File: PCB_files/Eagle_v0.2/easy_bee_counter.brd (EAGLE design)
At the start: 373.4 x 34.5 mm, 123 parts, among them Q6 60V/32A/35mΩ, Q7 60V/32A/35mΩ

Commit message: Converted Logo to library part Added vias to be solded bridged for jumpers to bypass the SIP resistors. Rerouted the board, realigned many of the parts.
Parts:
- added U$44: BEE_LOGO, owen_desktop:BEE_LOGO
- C7: value 1uF -> 0.1uF
- J1: value (none) -> S_5V
- J3: value (none) -> S_LOAD
- J4: value (none) -> S_I2C
- R11, R12, R2, R5, R6, R7: value (none) -> 100KΩ
- U$34, U$35, U$36, U$37: value RPACK-BUSSED-9 -> 22Ω
- U1, U2, U3, U4, U5, U6: value (none) -> 74*165
- U7: value (none) -> R78E3.3-1.0; device SparkFun-IC-Power:TO220-IGO -> SparkFun-IC-Power:DC-DC_CONVERTER_78XX
- moved R11 0.90 mm to (184.2, 6.99)
- moved U$113 0.76 mm to (157.1, 22.3)
- moved U$112 0.76 mm to (157.1, 18.2)
- moved U$100 0.75 mm to (233.3, 18.2)
- moved U$101 0.75 mm to (233.3, 22.3)
- moved U$98 0.67 mm to (246.0, 18.2)
- moved U$99 0.67 mm to (246.0, 22.3)
- moved U$109 0.65 mm to (182.5, 22.3)
- moved U$108 0.65 mm to (182.5, 18.2)
- moved U$80 0.62 mm to (360.3, 18.2)
- moved U$81 0.62 mm to (360.3, 22.3)
- moved U$107 0.61 mm to (195.2, 22.3)
- moved U$106 0.61 mm to (195.2, 18.2)
- moved U$96 0.60 mm to (258.7, 18.2)
- moved U$97 0.60 mm to (258.7, 22.3)
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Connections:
- removed net N$44: U$45.MOSI
- net 3.3V: now also U7.VOUT; no longer U7.OUT
- net 5V: now also U7.VIN; no longer U7.IN
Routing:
- net GND: track 773.0 -> 561.9 mm, vias 4 -> 1
- net 3.3V: track 734.0 -> 812.3 mm
- net N$112: track 68.9 -> 43.3 mm
- net N$141: track 66.1 -> 47.2 mm, vias 0 -> 2
- net N$40: track 66.4 -> 49.4 mm, vias 0 -> 1
- net N$35: track 64.2 -> 47.2 mm, vias 0 -> 1
- net N$108: track 57.1 -> 40.6 mm, vias 1 -> 0
- net N$43: track 60.6 -> 46.9 mm, vias 0 -> 1
- net N$105: track 46.5 -> 33.0 mm
- net N$12: track 40.8 -> 52.7 mm, vias 1 -> 0
- net N$117: track 51.2 -> 39.8 mm, vias 2 -> 0
- net N$27: track 37.4 -> 47.9 mm
- net N$93: track 43.9 -> 35.2 mm, vias 2 -> 0
- net SCL: track 77.8 -> 69.1 mm
- net N$37: track 42.6 -> 35.1 mm
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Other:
- board text added: "3v3"
- board text removed: "C:/Users/hydronics/Google Drive/2019/bee_counter/eagle/images/bmp_16/giant-honey-bee.bmp"

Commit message: Added jumpers for 13-24 (oops). Added Tkeepout areas to expose jumpers on component side.
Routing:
- net 23_CATHODE: track 10.3 -> 12.6 mm, vias 0 -> 1
- net 19_CATHODE: track 37.1 -> 39.3 mm, vias 0 -> 1
- net 24_CATHODE: track 20.8 -> 23.0 mm
- net N$21: track 299.1 -> 300.6 mm, vias 1 -> 13
- net 17_CATHODE: track 61.5 -> 60.4 mm, vias 0 -> 1
- net 22_CATHODE: track 8.42 -> 8.94 mm, vias 0 -> 1
- net 21_CATHODE: track 16.0 -> 16.4 mm, vias 0 -> 1
- net 14_CATHODE: track 8.69 -> 8.98 mm, vias 0 -> 1
- net 18_CATHODE: track 49.7 -> 49.8 mm, vias 0 -> 1
- net 20_CATHODE: vias 0 -> 1
- net 16_CATHODE: vias 0 -> 1
- net 15_CATHODE: vias 0 -> 1
- net 13_CATHODE: vias 0 -> 1

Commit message: cleaned up some additional errors.
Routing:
- net N$63: vias 13 -> 14
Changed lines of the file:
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@@
 <contactref element="U$91" pad="2"/>
 <contactref element="U$35" pad="P$5"/>
+<wire x1="307.34" y1="25.4" x2="312.42" y2="30.48" width="0.2032" layer="16"/>
+<via x="300.99" y="25.4" extent="1-16" drill="0.3302"/>
 <wire x1="298.799" y1="23.2266" x2="300.9724" y2="25.4" width="0.2032" layer="16"/>
-<wire x1="307.34" y1="25.4" x2="312.42" y2="30.48" width="0.2032" layer="16"/>
-<wire x1="300.9724" y1="25.4" x2="307.34" y2="25.4" width="0.2032" layer="16"/>
-<via x="300.99" y="25.4" extent="1-16" drill="0.3302"/>
-<wire x1="300.9724" y1="25.4" x2="300.99" y2="25.4" width="0" layer="19" extent="16-16"/>
+<wire x1="300.9724" y1="25.4" x2="300.99" y2="25.4" width="0.2032" layer="16"/>
+<wire x1="300.99" y1="25.4" x2="307.34" y2="25.4" width="0.2032" layer="16"/>
 </signal>
 <signal name="14_CATHODE">
@@
 <contactref element="U$87" pad="2"/>
 <contactref element="U$35" pad="P$3"/>
-<wire x1="324.199" y1="23.2266" x2="317.5" y2="29.9256" width="0.2032" layer="16"/>
-<wire x1="317.5" y1="29.9256" x2="317.5" y2="30.48" width="0.2032" layer="16"/>
 <via x="322.072" y="25.4" extent="1-16" drill="0.3302"/>
-<wire x1="322.072" y1="25.4" x2="324.199" y2="23.2266" width="0" layer="19" extent="1-1"/>
+<wire x1="324.199" y1="23.2266" x2="324.199" y2="23.273" width="0.2032" layer="16"/>
+<wire x1="324.199" y1="23.273" x2="322.072" y2="25.4" width="0.2032" layer="16"/>
+<wire x1="322.072" y1="25.4" x2="321.31" y2="25.4" width="0.2032" layer="16"/>
+<wire x1="321.31" y1="25.4" x2="317.5" y2="29.21" width="0.2032" layer="16"/>
+<wire x1="317.5" y1="29.21" x2="317.5" y2="30.48" width="0.2032" layer="16"/>
 </signal>
 <signal name="16_CATHODE">
@@
 <contactref element="U$83" pad="2"/>
 <contactref element="U$34" pad="P$9"/>
-<wire x1="349.599" y1="23.2266" x2="349.599" y2="25.3856" width="0.2032" layer="16"/>
 <wire x1="353.695" y1="31.115" x2="396.24" y2="31.115" width="0.2032" layer="16"/>
 <wire x1="396.24" y1="31.115" x2="398.145" y2="29.21" width="0.2032" layer="16"/>
 <wire x1="398.145" y1="29.21" x2="401.955" y2="29.21" width="0.2032" layer="16"/>
 <wire x1="401.955" y1="29.21" x2="403.225" y2="30.48" width="0.2032" layer="16"/>
+<wire x1="351.155" y1="26.8970125" x2="351.155" y2="28.575" width="0.2032" layer="16"/>
+<wire x1="351.155" y1="28.575" x2="353.695" y2="31.115" width="0.2032" layer="16"/>
 <via x="349.631" y="25.4" extent="1-16" drill="0.3302"/>
+<wire x1="349.599" y1="23.2266" x2="349.599" y2="25.368" width="0.2032" layer="16"/>
+<wire x1="349.599" y1="25.368" x2="349.631" y2="25.4" width="0.2032" layer="16"/>
+<wire x1="351.1280125" y1="26.8970125" x2="351.155" y2="26.8970125" width="0.2032" layer="16"/>
 <wire x1="349.631" y1="25.4" x2="349.8723" y2="25.6413" width="0.2032" layer="16"/>
 <wire x1="349.8723" y1="25.6413" x2="349.8992875" y2="25.6413" width="0.2032" layer="16"/>
-<wire x1="349.8992875" y1="25.6413" x2="351.155" y2="26.8970125" width="0.2032" layer="16"/>
-<wire x1="351.155" y1="26.8970125" x2="351.155" y2="28.575" width="0.2032" layer="16"/>
-<wire x1="351.155" y1="28.575" x2="353.695" y2="31.115" width="0.2032" layer="16"/>
-<wire x1="349.599" y1="25.3856" x2="349.631" y2="25.4" width="0" layer="19" extent="16-16"/>
+<wire x1="349.8992875" y1="25.6413" x2="350.2787" y2="26.0207125" width="0.2032" layer="16"/>
+<wire x1="350.2787" y1="26.0207125" x2="350.2787" y2="26.0477" width="0.2032" layer="16"/>
+<wire x1="350.2787" y1="26.0477" x2="351.1280125" y2="26.8970125" width="0.2032" layer="16"/>
 </signal>
 <signal name="18_CATHODE">
@@
 <contactref element="U$79" pad="2"/>
 <contactref element="U$34" pad="P$7"/>
-<wire x1="374.999" y1="23.2266" x2="375.126" y2="23.2266" width="0.2032" layer="16"/>
-<wire x1="377.2994" y1="25.4" x2="375.126" y2="23.2266" width="0.2032" layer="16"/>
 <wire x1="405.638" y1="26.543" x2="408.305" y2="29.21" width="0.2032" layer="16"/>
 <wire x1="408.305" y1="29.21" x2="408.305" y2="30.48" width="0.2032" layer="16"/>
-<wire x1="377.2994" y1="25.4" x2="379.73" y2="25.4" width="0.2032" layer="16"/>
 <wire x1="379.73" y1="25.4" x2="383.54" y2="29.21" width="0.2032" layer="16"/>
 <wire x1="383.54" y1="29.21" x2="393.7" y2="29.21" width="0.2032" layer="16"/>
@@
 <wire x1="401.447" y1="26.543" x2="405.638" y2="26.543" width="0.2032" layer="16"/>
 <via x="377.317" y="25.4" extent="1-16" drill="0.3302"/>
-<wire x1="377.2994" y1="25.4" x2="377.317" y2="25.4" width="0" layer="19" extent="16-16"/>
+<wire x1="374.999" y1="23.2266" x2="377.1724" y2="25.4" width="0.2032" layer="16"/>
+<wire x1="377.1724" y1="25.4" x2="377.317" y2="25.4" width="0.2032" layer="16"/>
+<wire x1="377.317" y1="25.4" x2="379.73" y2="25.4" width="0.2032" layer="16"/>
 </signal>
 <signal name="20_CATHODE">
@@
 <wire x1="140.589" y1="26.289" x2="147.955" y2="26.289" width="0.6096" layer="1"/>
 <via x="139.065" y="24.765" extent="1-16" drill="0.55"/>
-<wire x1="147.955" y1="26.289" x2="161.29" y2="26.289" width="0.6096" layer="1"/>
+<wire x1="147.955" y1="26.289" x2="158.496" y2="26.289" width="0.6096" layer="1"/>
+<wire x1="158.496" y1="26.289" x2="161.29" y2="26.289" width="0.6096" layer="1"/>
 <wire x1="161.29" y1="26.289" x2="173.99" y2="26.289" width="0.6096" layer="1"/>
 <wire x1="173.99" y1="26.289" x2="184.531" y2="26.289" width="0.6096" layer="1"/>
@@
 <via x="271.145" y="26.289" extent="1-16" drill="0.3302"/>
 <via x="273.05" y="26.289" extent="1-16" drill="0.3302"/>
+<via x="158.496" y="26.289" extent="1-16" drill="0.3302"/>
 </signal>
 <signal name="5V">
@@
 <via x="158.496" y="25.4" extent="1-16" drill="0.3302"/>
 </signal>
-<signal name="N$31">
-<via x="158.496" y="26.289" extent="1-16" drill="0.3302"/>
-</signal>
 </signals>

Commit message: Finalized all connections on schematic (missed some sensors last commit). Fully routed board using new component names and new pinouts for SIP packs.
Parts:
- removed U$100, U$101, U$102, U$103, U$104, U$105, U$106, U$107, U$108, U$109, U$110, U$111, U$112, U$113, U$114, U$115, U$68, U$69, U$70, U$71, U$72, U$73, U$74, U$75, U$76, U$77, U$78, U$79, U$80, U$81, U$82, U$83, U$84, U$85, U$86, U$87, U$88, U$89, U$90, U$91, U$92, U$93, U$94, U$95, U$96, U$97, U$98, U$99: QRE1113_, QRE1113:DIP400W50P180L360H200Q4
- added SERVO1, SERVO2, SERVO3, SERVO4, SERVO5: (no value), pinhead:1X03
- added U01I, U01O, U02I, U02O, U03I, U03O, U04I, U04O, U05I, U05O, U06I, U06O, U07I, U07O, U08I, U08O, U09I, U09O, U10I, U10O, U11I, U11O, U12I, U12O, U13I, U13O, U14I, U14O, U15I, U15O, U16I, U16O, U17I, U17O, U18I, U18O, U19I, U19O, U20I, U20O, U21I, U21O, U22I, U22O, U23I, U23O, U24I, U24O: QRE1113_QRE1113_, easy_bee_counter:QRE1113_DIP400W50P180L360H200Q4
- moved C1 59.7 mm to (381.6, 10.2), turned to 180 degrees
- moved C3 45.5 mm to (290.8, 10.2), turned to 180 degrees
- moved C2 44.3 mm to (344.8, 10.2), turned to 180 degrees
- moved C4 38.5 mm to (245.1, 10.2), turned to 180 degrees
- moved U$34 36.7 mm to (377.7, 17.8)
- moved U1 33.0 mm to (395.6, 6.35)
- moved C6 25.9 mm to (151.1, 9.53), turned to 180 degrees
- moved C5 23.6 mm to (206.4, 10.2), turned to 180 degrees
- moved R11 21.3 mm to (203.2, 16.5)
- moved U3 19.7 mm to (304.2, 6.35)
- moved U$35 18.9 mm to (324.5, 17.1)
- moved U2 18.4 mm to (358.1, 6.35)
- moved U$37 17.0 mm to (275.5, 18.4)
- moved R7 16.6 mm to (226.7, 17.8)
- moved R12 15.1 mm to (144.8, 16.5)
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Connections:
- net N$21 renamed PWR_13-24
- net N$63 renamed PWR_1-12
- removed net N$101: R12.P$4, U$112.4, U6.13
- removed net N$102: R12.P$5, U$113.4, U6.14
- removed net N$105: R11.P$5, U$105.4, U5.14
- removed net N$108: R12.P$8, U$108.4, U6.5
- removed net N$109: R12.P$9, U$109.4, U6.6
- removed net N$112: R11.P$9, U$101.4, U5.6
- removed net N$117: R11.P$7, U$103.4, U5.4
- removed net N$12: R5.P$9, U$77.4, U2.6
- removed net N$131: R7.P$5, U$97.4, U4.14
- removed net N$135: R7.P$9, U$93.4, U4.6
- removed net N$140: R7.P$7, U$95.4, U4.4
- removed net N$141: R7.P$3, U$99.4, U4.12
- removed net N$15: R6.P$3, U$90.4, U3.11
- removed net N$16: R6.P$2, U$91.4, U3.12
- removed net N$17: R6.P$4, U$88.4, U3.13
- removed net N$18: R12.P$6, U$110.4, U6.3
- removed net N$19: R6.P$5, U$89.4, U3.14
- removed net N$20: R6.P$8, U$84.4, U3.5
- removed net N$22: R6.P$9, U$85.4, U3.6
- removed net N$23: R6.P$6, U$86.4, U3.3
- removed net N$24: R6.P$7, U$87.4, U3.4
- removed net N$25: R5.P$4, U$80.4, U2.13
- removed net N$26: R5.P$5, U$81.4, U2.14
- removed net N$27: R5.P$8, U$76.4, U2.5
- removed net N$28: U3.9, U4.10
- removed net N$29: R5.P$6, U$78.4, U2.3
- removed net N$30: R12.P$3, U$114.4, U6.11
- removed net N$32: R5.P$7, U$79.4, U2.4
- removed net N$33: R5.P$3, U$83.4, U2.12
- removed net N$34: R7.P$4, U$96.4, U4.13
- removed net N$35: R5.P$2, U$82.4, U2.11
- removed net N$36: R2.P$7, U$72.4, U1.13
- removed net N$37: R2.P$6, U$73.4, U1.14
- removed net N$38: R2.P$5, U$68.4, U1.5
- removed net N$39: R2.P$4, U$69.4, U1.6
- removed net N$40: R2.P$2, U$70.4, U1.3
- removed net N$41: R2.P$3, U$71.4, U1.4
- removed net N$42: R2.P$8, U$75.4, U1.12
- removed net N$43: R2.P$9, U$74.4, U1.11
- removed net N$58: R12.P$7, U$111.4, U6.4
- removed net N$62: R7.P$8, U$92.4, U4.5
- removed net N$65: R7.P$6, U$94.4, U4.3
- removed net N$68: R7.P$2, U$98.4, U4.11
- removed net N$74: R11.P$3, U$107.4, U5.12
- removed net N$87: R12.P$2, U$115.4, U6.12
- removed net N$89: R11.P$4, U$104.4, U5.13
- removed net N$91: R11.P$8, U$100.4, U5.5
- removed net N$93: R11.P$6, U$102.4, U5.3
- removed net N$97: R11.P$2, U$106.4, U5.11
- new net SER5: U1.9, U2.10
- new net SNS01I: R12.P$3, U01I.4, U6.4
- new net SNS01O: R12.P$2, U01O.4, U6.3
- new net SNS02I: R12.P$5, U02I.4, U6.6
- new net SNS02O: R12.P$4, U02O.4, U6.5
- new net SNS03I: R12.P$7, U03I.4, U6.13
- new net SNS03O: R12.P$6, U03O.4, U6.14
- new net SNS04I: R12.P$9, U04I.4, U6.11
- new net SNS04O: R12.P$8, U04O.4, U6.12
- new net SNS05I: R11.P$3, U05I.4, U5.4
- new net SNS05O: R11.P$2, U05O.4, U5.3
- new net SNS06I: R11.P$5, U06I.4, U5.6
- new net SNS06O: R11.P$4, U06O.4, U5.5
- new net SNS07I: R11.P$7, U07I.4, U5.13
- new net SNS07O: R11.P$6, U07O.4, U5.14
- new net SNS08I: R11.P$9, U08I.4, U5.11
- new net SNS08O: R11.P$8, U08O.4, U5.12
- new net SNS09I: R7.P$3, U09I.4, U4.4
- new net SNS09O: R7.P$2, U09O.4, U4.3
- new net SNS10I: R7.P$5, U10I.4, U4.6
- new net SNS10O: R7.P$4, U10O.4, U4.5
- new net SNS11I: R7.P$7, U11I.4, U4.13
- new net SNS11O: R7.P$6, U11O.4, U4.14
- new net SNS12I: R7.P$9, U12I.4, U4.11
- new net SNS12O: R7.P$8, U12O.4, U4.12
- new net SNS13I: R6.P$3, U13I.4, U3.4
- new net SNS13O: R6.P$2, U13O.4, U3.3
- new net SNS14I: R6.P$5, U14I.4, U3.6
- new net SNS14O: R6.P$4, U14O.4, U3.5
- new net SNS15I: R6.P$7, U15I.4, U3.13
- new net SNS15O: R6.P$6, U15O.4, U3.14
- new net SNS16I: R6.P$9, U16I.4, U3.11
- new net SNS16O: R6.P$8, U16O.4, U3.12
- new net SNS17I: R5.P$3, U17I.4, U2.4
- new net SNS17O: R5.P$2, U17O.4, U2.3
- new net SNS18I: R5.P$5, U18I.4, U2.6
- new net SNS18O: R5.P$4, U18O.4, U2.5
- new net SNS19I: R5.P$7, U19I.4, U2.13
- new net SNS19O: R5.P$6, U19O.4, U2.14
- new net SNS20I: R5.P$9, U2.11, U20I.4
- new net SNS20O: R5.P$8, U2.12, U20O.4
- new net SNS21I: R2.P$3, U1.4, U21I.4
- new net SNS21O: R2.P$2, U1.3, U21O.4
- new net SNS22I: R2.P$5, U1.6, U22I.4
- new net SNS22O: R2.P$4, U1.5, U22O.4
- new net SNS23I: R2.P$7, U1.13, U23I.4
- new net SNS23O: R2.P$6, U1.14, U23O.4
- new net SNS24I: R2.P$9, U1.11, U24I.4
- new net SNS24O: R2.P$8, U1.12, U24O.4
- new net SRVO1: MS2.5, SERVO1.3, U$45.A0
- new net SRVO2: MS2.6, SERVO2.3, U$45.A1
- new net SRVO3: MS2.7, SERVO3.3, U$45.A2
- new net SRVO4: MS2.25, SERVO4.3, U$45.D13
- new net SRVO5: MS2.24, SERVO5.3, U$45.D9
- net 10_CATHODE: now also U10O.2; no longer U$97.2
- net 11_CATHODE: now also U11O.2; no longer U$95.2
- net 12_CATHODE: now also U12O.2; no longer U$93.2
- net 13_CATHODE: now also U13O.2; no longer U$91.2
- net 14_CATHODE: now also U14O.2; no longer U$89.2
- net 15_CATHODE: now also U15O.2; no longer U$87.2
- net 16_CATHODE: now also U16O.2; no longer U$85.2
- net 17_CATHODE: now also U17O.2; no longer U$83.2
- net 18_CATHODE: now also U18O.2; no longer U$81.2
- net 19_CATHODE: now also U19O.2; no longer U$79.2
- net 1_CATHODE: now also U01O.2; no longer U$115.2
- net 20_CATHODE: now also U20O.2; no longer U$77.2
- net 21_CATHODE: now also U21O.2; no longer U$75.2
- net 22_CATHODE: now also U22O.2; no longer U$73.2
- net 23_CATHODE: now also U23O.2; no longer U$71.2
- net 24_CATHODE: now also U24O.2; no longer U$69.2
- net 2_CATHODE: now also U02O.2; no longer U$113.2
- net 3.3V: now also U01I.1, U01I.3, U01O.3, U02I.1, U02I.3, U02O.3, U03I.1, U03I.3, U03O.3, U04I.1, U04I.3, U04O.3, U05I.1, U05I.3, U05O.3, U06I.1, U06I.3, U06O.3, U07I.1, U07I.3, U07O.3, U08I.1, U08I.3, U08O.3, U09I.1, U09I.3, U09O.3, U10I.1, U10I.3, U10O.3, U11I.1, U11I.3, U11O.3, U12I.1, U12I.3, U12O.3, U13I.1, U13I.3, U13O.3, U14I.1, U14I.3, U14O.3, U15I.1, U15I.3, U15O.3, U16I.1, U16I.3, U16O.3, U17I.1, U17I.3, U17O.3, U18I.1, U18I.3, U18O.3, U19I.1, U19I.3, U19O.3, U20I.1, U20I.3, U20O.3, U21I.1, U21I.3, U21O.3, U22I.1, U22I.3, U22O.3, U23I.1, U23I.3, U23O.3, U24I.1, U24I.3, U24O.3; no longer U$100.1, U$100.3, U$101.3, U$102.1, U$102.3, U$103.3, U$104.1, U$104.3, U$105.3, U$106.1, U$106.3, U$107.3, U$108.1, U$108.3, U$109.3, U$110.1, U$110.3, U$111.3, U$112.1, U$112.3, U$113.3, U$114.1, U$114.3, U$115.3, U$68.1, U$68.3, U$69.3, U$70.1, U$70.3, U$71.3, U$72.1, U$72.3, U$73.3, U$74.1, U$74.3, U$75.3, U$76.1, U$76.3, U$77.3, U$78.1, U$78.3, U$79.3, U$80.1, U$80.3, U$81.3, U$82.1, U$82.3, U$83.3, U$84.1, U$84.3, U$85.3, U$86.1, U$86.3, U$87.3, U$88.1, U$88.3, U$89.3, U$90.1, U$90.3, U$91.3, U$92.1, U$92.3, U$93.3, U$94.1, U$94.3, U$95.3, U$96.1, U$96.3, U$97.3, U$98.1, U$98.3, U$99.3
- net 3_CATHODE: now also U03O.2; no longer U$111.2
- net 4_CATHODE: now also U04O.2; no longer U$109.2
- net 5V: now also SERVO1.2, SERVO2.2, SERVO3.2, SERVO4.2, SERVO5.2
- net 5_CATHODE: now also U05O.2; no longer U$107.2
- net 6_CATHODE: now also U06O.2; no longer U$105.2
- net 7_CATHODE: now also U07O.2; no longer U$103.2
- net 8_CATHODE: now also U08O.2; no longer U$101.2
- net 9_CATHODE: now also U09O.2; no longer U$99.2
- net GND: now also SERVO1.1, SERVO2.1, SERVO3.1, SERVO4.1, SERVO5.1
- net N$1: now also U11I.2, U11O.1; no longer U$94.2, U$95.1
- net N$10: now also U07I.2, U07O.1; no longer U$102.2, U$103.1
- net N$11: now also U03I.2, U03O.1; no longer U$110.2, U$111.1
- net N$13: now also U02I.2, U02O.1; no longer U$112.2, U$113.1
- net N$14: now also U01I.2, U01O.1; no longer U$114.2, U$115.1
- net N$2: now also U12I.2, U12O.1; no longer U$92.2, U$93.1
- net N$3: now also U10I.2, U10O.1; no longer U$96.2, U$97.1
- net N$4: now also U09I.2, U09O.1; no longer U$98.2, U$99.1
- net N$45: now also U24I.2, U24O.1; no longer U$68.2, U$69.1
- net N$46: now also U23I.2, U23O.1; no longer U$70.2, U$71.1
- net N$47: now also U22I.2, U22O.1; no longer U$72.2, U$73.1
- net N$48: now also U21I.2, U21O.1; no longer U$74.2, U$75.1
- net N$49: now also U17I.2, U17O.1; no longer U$82.2, U$83.1
- net N$5: now also U05I.2, U05O.1; no longer U$106.2, U$107.1
- net N$50: now also U18I.2, U18O.1; no longer U$80.2, U$81.1
- net N$51: now also U20I.2, U20O.1; no longer U$76.2, U$77.1
- net N$52: now also U19I.2, U19O.1; no longer U$78.2, U$79.1
- net N$53: now also U16I.2, U16O.1; no longer U$84.2, U$85.1
- net N$54: now also U15I.2, U15O.1; no longer U$86.2, U$87.1
- net N$55: now also U14I.2, U14O.1; no longer U$88.2, U$89.1
- net N$56: now also U13I.2, U13O.1; no longer U$90.2, U$91.1
- net N$6: now also U06I.2, U06O.1; no longer U$104.2, U$105.1
- net N$7: now also U08I.2, U08O.1; no longer U$100.2, U$101.1
- net N$8: now also U04I.2, U04O.1; no longer U$108.2, U$109.1
- net SER3: now also U3.9, U4.10; no longer U2.9, U3.10
- net SER4: now also U2.9, U3.10; no longer U1.9, U2.10
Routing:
- net SRVO1: track 0.00 -> 366.2 mm, vias 0 -> 1
- net SRVO2: track 0.00 -> 349.4 mm, vias 0 -> 2
- net SRVO3: track 0.00 -> 341.0 mm, vias 0 -> 1
- net 5V: track 63.4 -> 374.9 mm, vias 0 -> 1
- net SRVO4: track 0.00 -> 283.4 mm, vias 0 -> 2
- net 3.3V: track 812.3 -> 647.2 mm, vias 3 -> 2
- net SRVO5: track 0.00 -> 126.1 mm, vias 0 -> 5
- net SNS12O: track 0.00 -> 63.8 mm
- net SNS10O: track 0.00 -> 60.7 mm
- net N$28: track 59.3 -> 0.00 mm, vias 1 -> 0
- net N$39: track 56.3 -> 0.00 mm, vias 1 -> 0
- net SNS10I: track 0.00 -> 56.0 mm
- net N$41: track 55.7 -> 0.00 mm, vias 1 -> 0
- net SNS09O: track 0.00 -> 54.6 mm
- net SNS11O: track 0.00 -> 53.5 mm, vias 0 -> 1
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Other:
- board size 373.4 x 34.5 mm -> 373.4 x 38.4 mm
- board text added: "This side out"
- board text added: "This side towards Hive"

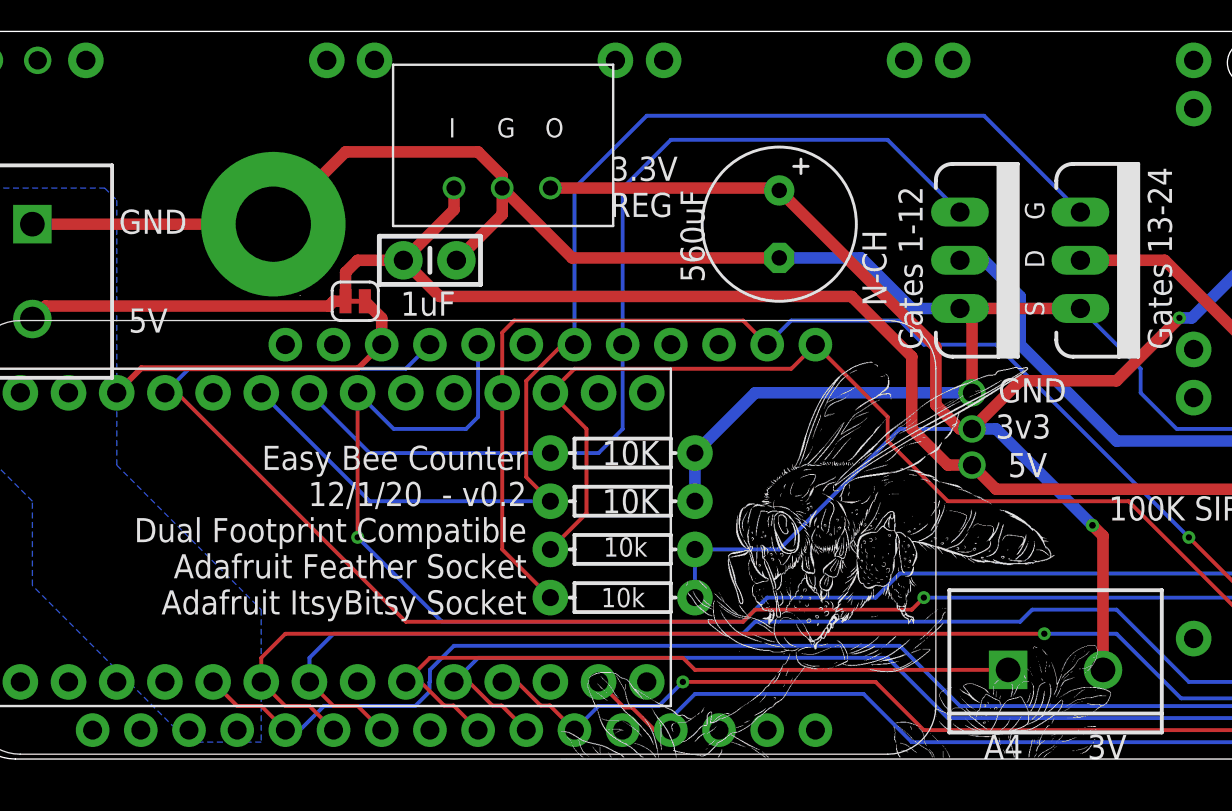
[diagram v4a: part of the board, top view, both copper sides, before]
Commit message: Corrected unusable pins for servos
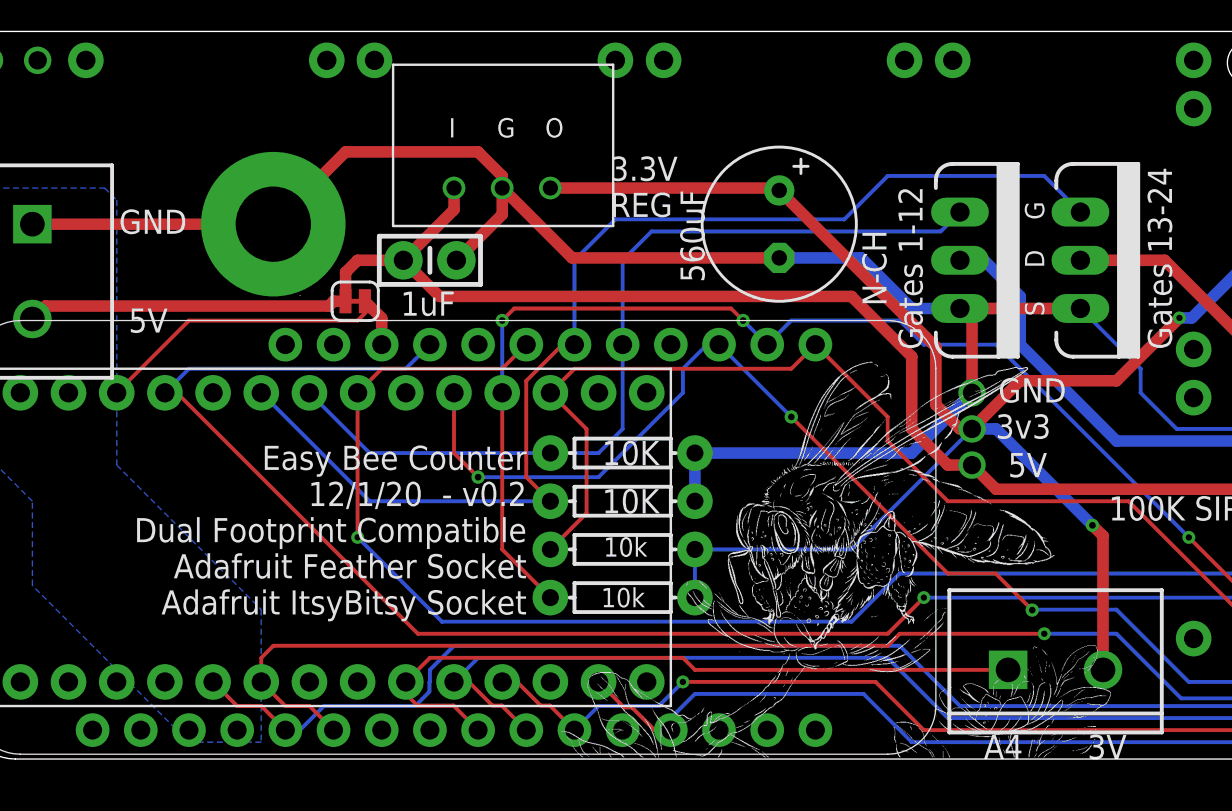
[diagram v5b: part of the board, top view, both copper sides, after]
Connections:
- net SRVO3: now also MS2.19, U$45.D5; no longer MS2.7, U$45.A2
- net SRVO5: now also MS2.23; no longer MS2.24
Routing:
- net P1: track 51.5 -> 46.1 mm
- net P2: track 66.4 -> 61.6 mm
- net SRVO3: track 341.0 -> 339.3 mm, vias 1 -> 4
- net SRVO5: track 126.1 -> 124.8 mm
- net SCL: track 71.7 -> 72.6 mm, vias 1 -> 3
- net SRVO4: track 283.4 -> 283.9 mm
